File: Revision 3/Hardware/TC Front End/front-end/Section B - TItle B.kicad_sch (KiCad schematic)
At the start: 17 parts, among them J1 Conn_01x02, J2 Conn_01x02, J3 Conn_01x02, U1 LM321, U2 LM321

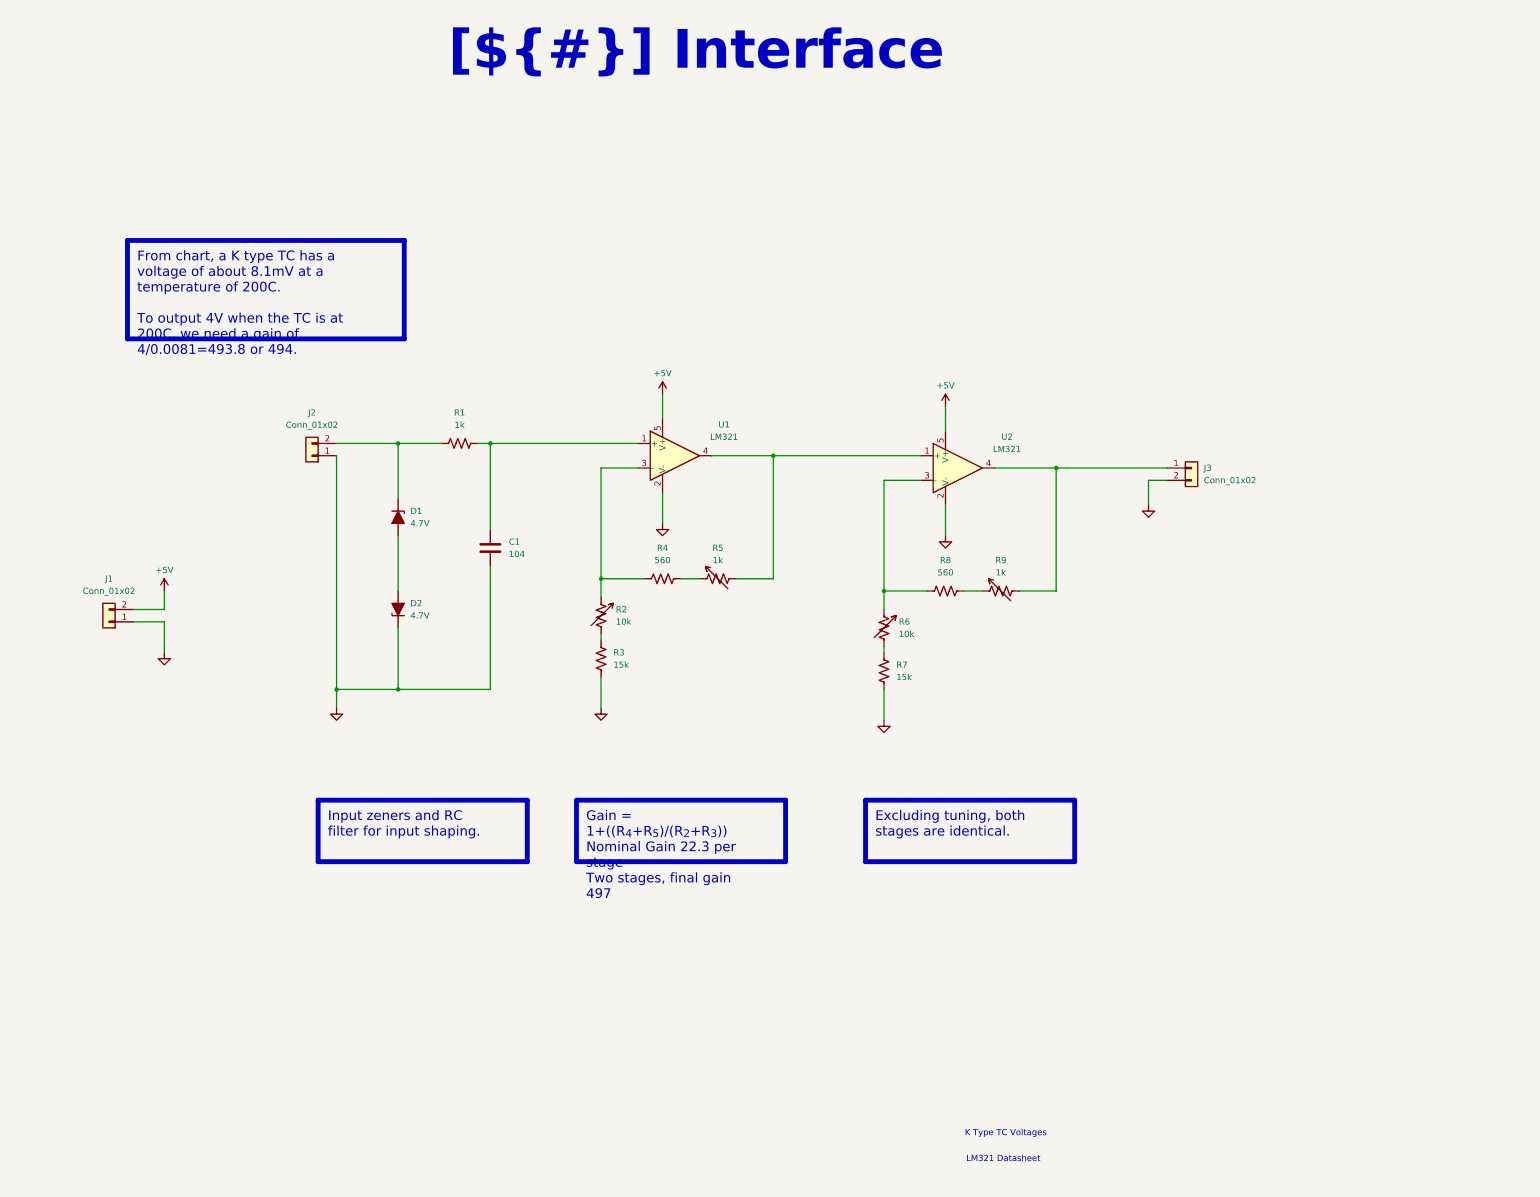
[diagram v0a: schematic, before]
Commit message: Add footprints to schematic
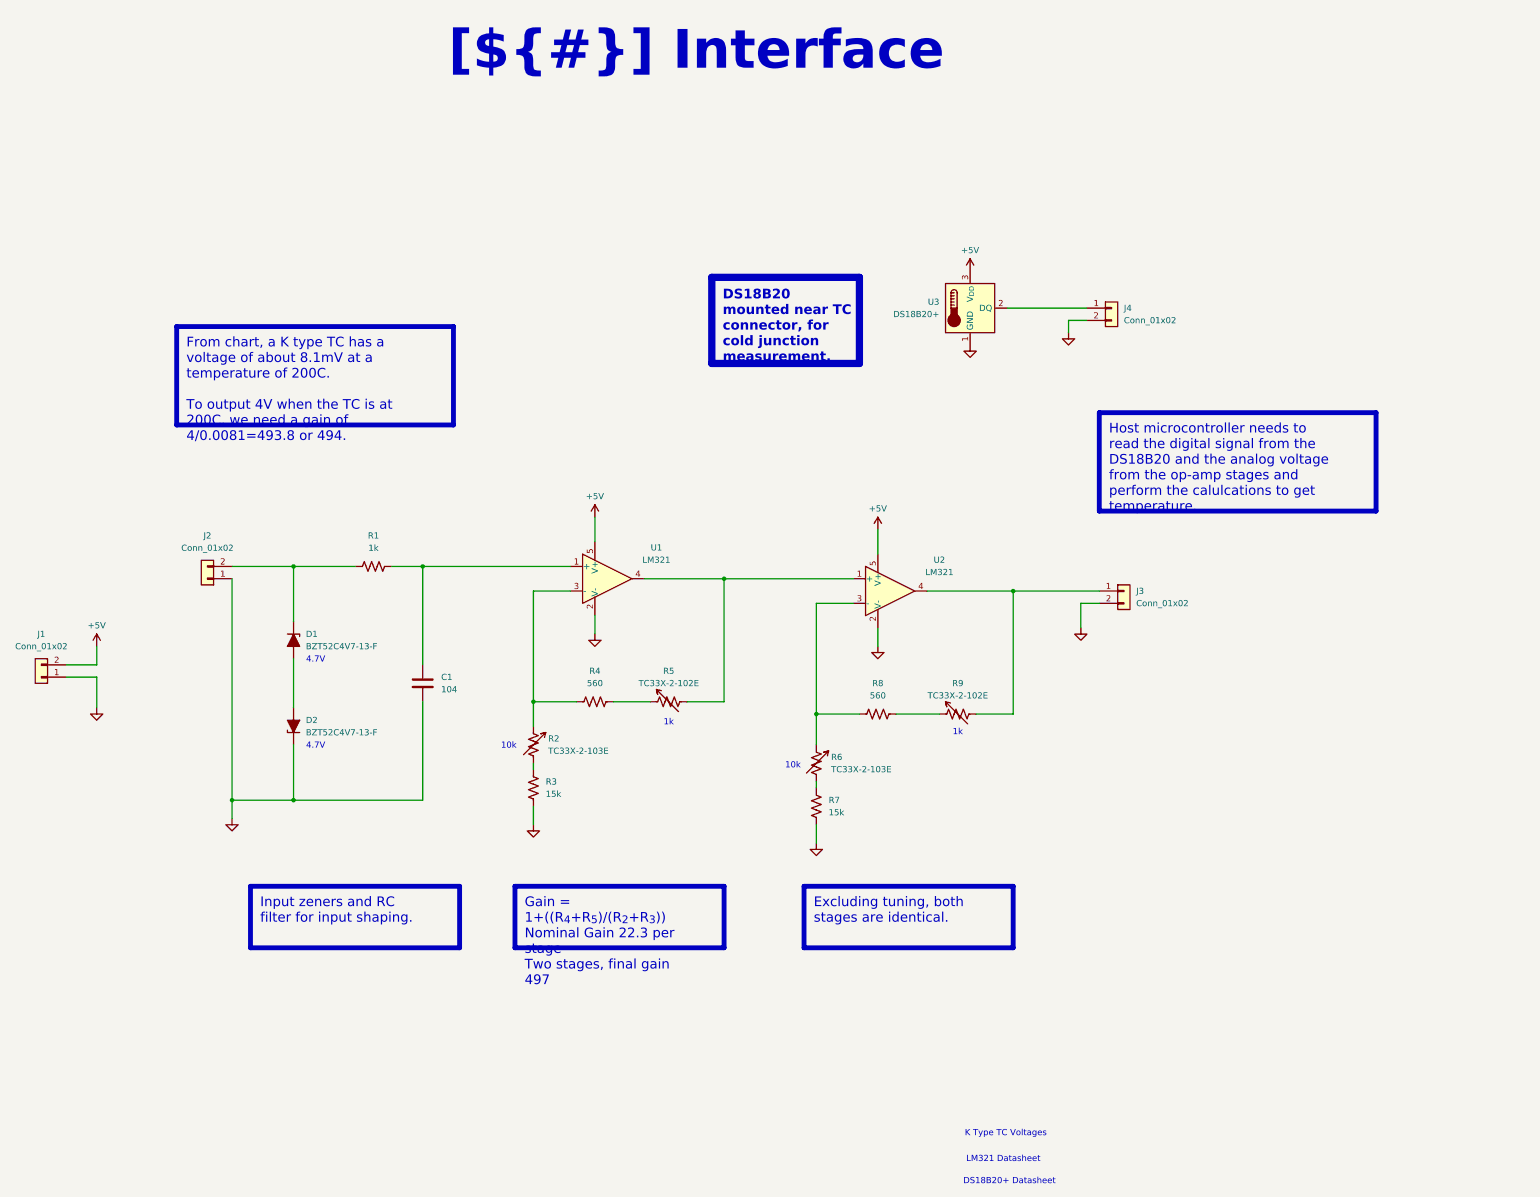
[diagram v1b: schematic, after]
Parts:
- added J4: Conn_01x02, Connector_PinHeader_2.54mm:PinHeader_1x02_P2.54mm_Vertical, symbol Connector_Generic:Conn_01x02
- added U3: DS18B20+, Package_TO_SOT_THT:TO-92_Inline, symbol Sensor_Temperature:DS18B20
- C1: footprint (none) -> Capacitor_SMD:C_0603_1608Metric_Pad1.08x0.95mm_HandSolder
- D1, D2: value 4.7V -> BZT52C4V7-13-F; footprint (none) -> Diode_SMD:D_SOD-123
- J1, J2, J3: footprint (none) -> Connector_PinHeader_2.54mm:PinHeader_1x02_P2.54mm_Vertical
- R1, R3, R4, R7, R8: footprint (none) -> Resistor_SMD:R_0603_1608Metric_Pad0.98x0.95mm_HandSolder
- R2, R6: value 10k -> TC33X-2-103E; footprint (none) -> Potentiometer_SMD:Potentiometer_Bourns_TC33X_Vertical
- R5, R9: value 1k -> TC33X-2-102E; footprint (none) -> Potentiometer_SMD:Potentiometer_Bourns_TC33X_Vertical
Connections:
- net +5V: now also U3.3 (V_{DD})
- net GND: now also J4.2 (Pin_2), U3.1 (GND)
- new net: J4.1 (Pin_1), U3.2 (DQ)
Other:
- note added: "10k"
- note added: "1k"
- note added: "4.7V"
- note added: "DS18B20+ Datasheet"
- moved on the sheet: C1, D1, D2, J1, J2, J3, R1, R2, R3, R4, R5, R6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

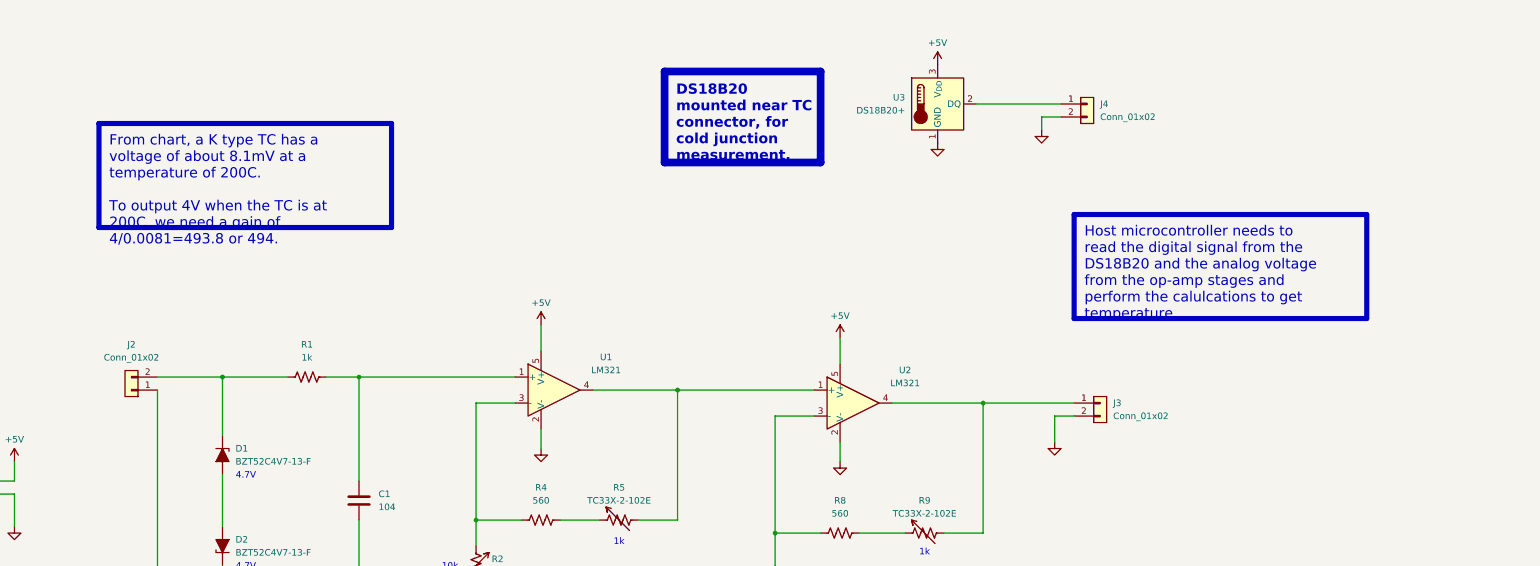
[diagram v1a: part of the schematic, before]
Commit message: Add parts to PCB and get models. Layout can now begin
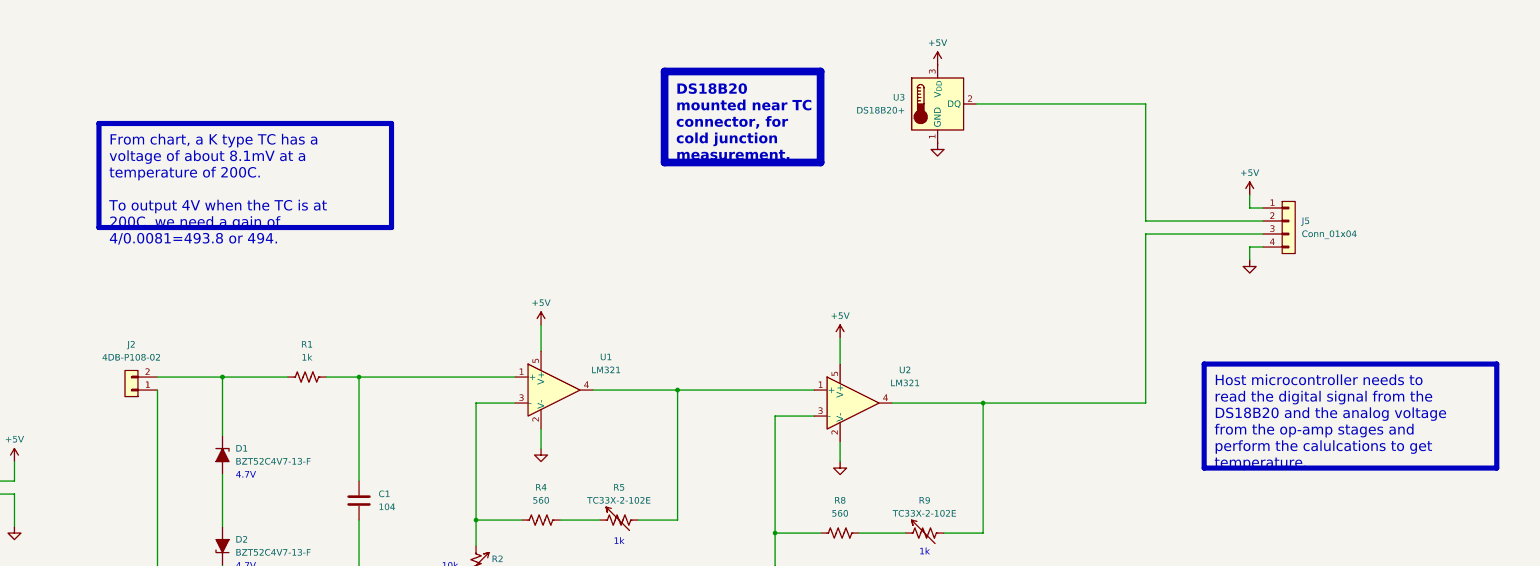
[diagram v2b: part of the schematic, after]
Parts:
- removed J3, J4: Conn_01x02, Connector_PinHeader_2.54mm:PinHeader_1x02_P2.54mm_Vertical, symbol Connector_Generic:Conn_01x02
- added J5: Conn_01x04, Connector_PinHeader_2.54mm:PinHeader_1x04_P2.54mm_Vertical, symbol Connector_Generic:Conn_01x04
- J1: footprint Connector_PinHeader_2.54mm:PinHeader_1x02_P2.54mm_Vertical -> TerminalBlock_Phoenix:TerminalBlock_Phoenix_MKDS-1,5-2_1x02_P5.00mm_Horizontal
- J2: value Conn_01x02 -> 4DB-P108-02; footprint Connector_PinHeader_2.54mm:PinHeader_1x02_P2.54mm_Vertical -> 4DB_P108_02:CONN_4DB-P108-02_TEC
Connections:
- net +5V: now also J5.1 (Pin_1)
- net GND: now also J5.4 (Pin_4)
- net at U3.2 (DQ): now also J5.2 (Pin_2)
- net at R9.2, U2.4: now also J5.3 (Pin_3)
